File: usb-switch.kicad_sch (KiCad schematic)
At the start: 4 parts, among them U17 FSUSB42UMX

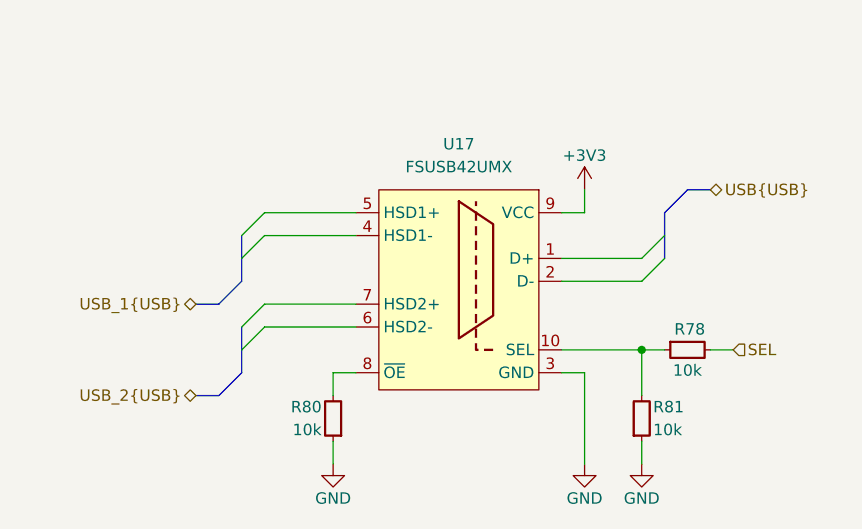
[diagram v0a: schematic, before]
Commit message: [#3] Layout HDMI, PCIe and ETH differential pairs
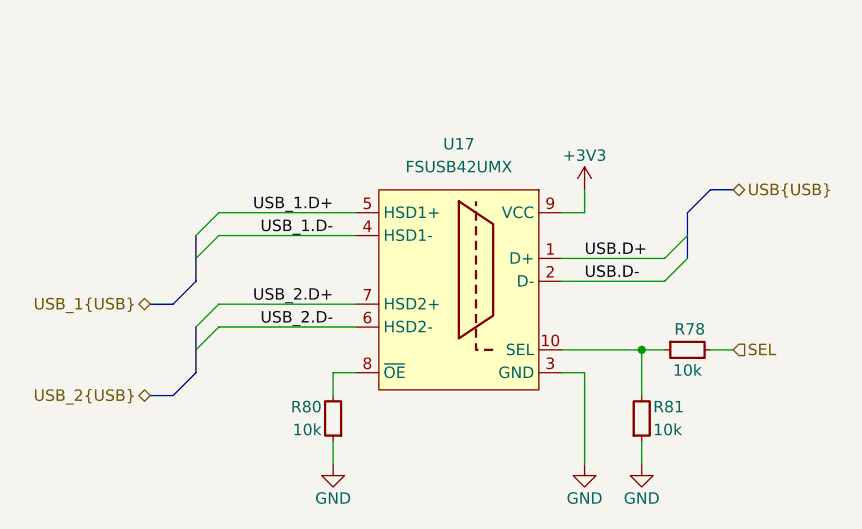
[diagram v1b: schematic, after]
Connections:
- net USB.D+: now reaches U17.1 (D+)
- net USB.D-: now reaches U17.2 (D-)
- net USB_1.D-: now reaches U17.4 (HSD1-)
- net USB_1.D+: now reaches U17.5 (HSD1+)
- net USB_2.D-: now reaches U17.6 (HSD2-)
- net USB_2.D+: now reaches U17.7 (HSD2+)
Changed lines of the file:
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@@
 	)
 	(bus_entry
-		(at 106.68 111.76)
+		(at 101.6 111.76)
 		(size 2.54 -2.54)
 		(stroke
@@
 	)
 	(bus_entry
-		(at 153.67 101.6)
+		(at 156.21 101.6)
 		(size -2.54 2.54)
 		(stroke
@@
 	)
 	(bus_entry
-		(at 153.67 104.14)
+		(at 156.21 104.14)
 		(size -2.54 2.54)
 		(stroke
@@
 	)
 	(bus_entry
-		(at 106.68 104.14)
+		(at 101.6 104.14)
 		(size 2.54 -2.54)
 		(stroke
@@
 	)
 	(bus_entry
-		(at 106.68 114.3)
+		(at 101.6 114.3)
 		(size 2.54 -2.54)
 		(stroke
@@
 	)
 	(bus_entry
-		(at 106.68 101.6)
+		(at 101.6 101.6)
 		(size 2.54 -2.54)
 		(stroke
@@
 	(bus
 		(pts
-			(xy 106.68 114.3) (xy 106.68 116.84)
-		)
-		(stroke
-			(width 0)
-			(type default)
-		)
-	)
-	(wire
-		(pts
-			(xy 142.24 106.68) (xy 151.13 106.68)
+			(xy 101.6 114.3) (xy 101.6 116.84)
+		)
+		(stroke
+			(width 0)
+			(type default)
+		)
+	)
+	(wire
+		(pts
+			(xy 142.24 106.68) (xy 153.67 106.68)
 		)
 		(stroke
@@
 	(wire
 		(pts
-			(xy 109.22 109.22) (xy 119.38 109.22)
-		)
-		(stroke
-			(width 0)
-			(type default)
-		)
-	)
-	(bus
-		(pts
-			(xy 106.68 104.14) (xy 106.68 106.68)
-		)
-		(stroke
-			(width 0)
-			(type default)
-		)
-	)
-	(bus
-		(pts
-			(xy 158.75 96.52) (xy 156.21 96.52)
-		)
-		(stroke
-			(width 0)
-			(type default)
-		)
-	)
-	(bus
-		(pts
-			(xy 106.68 101.6) (xy 106.68 104.14)
+			(xy 104.14 109.22) (xy 119.38 109.22)
+		)
+		(stroke
+			(width 0)
+			(type default)
+		)
+	)
+	(bus
+		(pts
+			(xy 161.29 96.52) (xy 158.75 96.52)
+		)
+		(stroke
+			(width 0)
+			(type default)
+		)
+	)
+	(bus
+		(pts
+			(xy 101.6 101.6) (xy 101.6 104.14)
 		)
 		(stroke
@@
 	(bus
 		(pts
-			(xy 101.6 119.38) (xy 104.14 119.38)
+			(xy 96.52 119.38) (xy 99.06 119.38)
 		)
 		(stroke
@@
 	(bus
 		(pts
-			(xy 101.6 109.22) (xy 104.14 109.22)
-		)
-		(stroke
-			(width 0)
-			(type default)
-		)
-	)
-	(bus
-		(pts
-			(xy 104.14 109.22) (xy 106.68 106.68)
-		)
-		(stroke
-			(width 0)
-			(type default)
-		)
-	)
-	(bus
-		(pts
-			(xy 104.14 119.38) (xy 106.68 116.84)
+			(xy 96.52 109.22) (xy 99.06 109.22)
+		)
+		(stroke
+			(width 0)
+			(type default)
+		)
+	)
+	(bus
+		(pts
+			(xy 99.06 109.22) (xy 101.6 106.68)
+		)
+		(stroke
+			(width 0)
+			(type default)
+		)
+	)
+	(bus
+		(pts
+			(xy 99.06 119.38) (xy 101.6 116.84)
 		)
 		(stroke
@@
 	(wire
 		(pts
-			(xy 109.22 111.76) (xy 119.38 111.76)
-		)
-		(stroke
-			(width 0)
-			(type default)
-		)
-	)
-	(bus
-		(pts
-			(xy 153.67 101.6) (xy 153.67 99.06)
-		)
-		(stroke
-			(width 0)
-			(type default)
-		)
-	)
-	(wire
-		(pts
-			(xy 142.24 104.14) (xy 151.13 104.14)
-		)
-		(stroke
-			(width 0)
-			(type default)
-		)
-	)
-	(wire
-		(pts
-			(xy 109.22 99.06) (xy 119.38 99.06)
-		)
-		(stroke
-			(width 0)
-			(type default)
-		)
-	)
-	(bus
-		(pts
-			(xy 153.67 104.14) (xy 153.67 101.6)
+			(xy 104.14 111.76) (xy 119.38 111.76)
+		)
+		(stroke
+			(width 0)
+			(type default)
+		)
+	)
+	(bus
+		(pts
+			(xy 156.21 101.6) (xy 156.21 99.06)
+		)
+		(stroke
+			(width 0)
+			(type default)
+		)
+	)
+	(wire
+		(pts
+			(xy 142.24 104.14) (xy 153.67 104.14)
+		)
+		(stroke
+			(width 0)
+			(type default)
+		)
+	)
+	(wire
+		(pts
+			(xy 104.14 99.06) (xy 119.38 99.06)
+		)
+		(stroke
+			(width 0)
+			(type default)
+		)
+	)
+	(bus
+		(pts
+			(xy 156.21 104.14) (xy 156.21 101.6)
+		)
+		(stroke
+			(width 0)
+			(type default)
+		)
+	)
+	(bus
+		(pts
+			(xy 101.6 104.14) (xy 101.6 106.68)
 		)
 		(stroke
@@
 	(bus
 		(pts
-			(xy 106.68 111.76) (xy 106.68 114.3)
-		)
-		(stroke
-			(width 0)
-			(type default)
-		)
-	)
-	(bus
-		(pts
-			(xy 156.21 96.52) (xy 153.67 99.06)
+			(xy 101.6 111.76) (xy 101.6 114.3)
+		)
+		(stroke
+			(width 0)
+			(type default)
+		)
+	)
+	(bus
+		(pts
+			(xy 158.75 96.52) (xy 156.21 99.06)
 		)
 		(stroke
@@
 	(wire
 		(pts
-			(xy 109.22 101.6) (xy 119.38 101.6)
+			(xy 104.14 101.6) (xy 119.38 101.6)
 		)
 		(stroke
@@
 			(width 0)
 			(type default)
+		)
+	)
+	(label "USB.D+"
+		(at 144.78 104.14 0)
+		(effects
+			(font
+				(size 1.27 1.27)
+			)
+			(justify left bottom)
+		)
+	)
+	(label "USB_1.D+"
+		(at 116.84 99.06 180)
+		(effects
+			(font
+				(size 1.27 1.27)
+			)
+			(justify right bottom)
+		)
+	)
+	(label "USB_1.D-"
+		(at 116.84 101.6 180)
+		(effects
+			(font
+				(size 1.27 1.27)
+			)
+			(justify right bottom)
+		)
+	)
+	(label "USB_2.D+"
+		(at 116.84 109.22 180)
+		(effects
+			(font
+				(size 1.27 1.27)
+			)
+			(justify right bottom)
+		)
+	)
+	(label "USB.D-"
+		(at 144.78 106.68 0)
+		(effects
+			(font
+				(size 1.27 1.27)
+			)
+			(justify left bottom)
+		)
+	)
+	(label "USB_2.D-"
+		(at 116.84 111.76 180)
+		(effects
+			(font
+				(size 1.27 1.27)
+			)
+			(justify right bottom)
 		)
 	)
 	(hierarchical_label "USB_1{USB}"
 		(shape bidirectional)
-		(at 101.6 109.22 180)
+		(at 96.52 109.22 180)
 		(effects
 			(font
@@
 	(hierarchical_label "USB_2{USB}"
 		(shape bidirectional)
-		(at 101.6 119.38 180)
+		(at 96.52 119.38 180)
 		(effects
 			(font
@@
 	(hierarchical_label "USB{USB}"
 		(shape bidirectional)
-		(at 158.75 96.52 0)
-		(effects
-			(font
+		(at 161.29 96.52 0)
+		(effects
+			(font

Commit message: [#3] Continue layout, minor schematic fixes, add power switch for CAN transceiver 5V rail
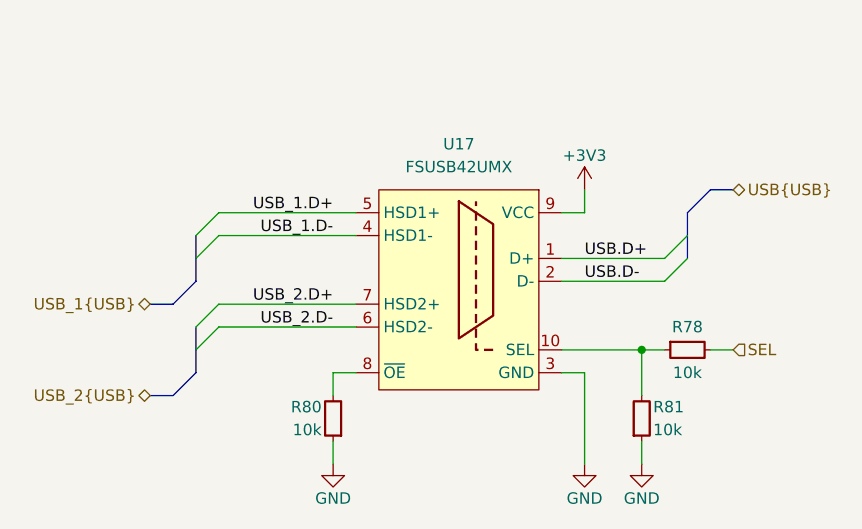
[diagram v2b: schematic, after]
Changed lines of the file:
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@@
 		(dnp no)
 		(property "Reference" "R78"
-			(at 156.464 112.014 0)
+			(at 156.21 111.76 0)
 			(effects
 				(font
@@
 		)
 		(property "Val" "10k"
-			(at 156.21 116.586 0)
+			(at 156.21 116.84 0)
 			(effects
 				(font

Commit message: [#3] WIP: Clear ERC, re-annotate schematic
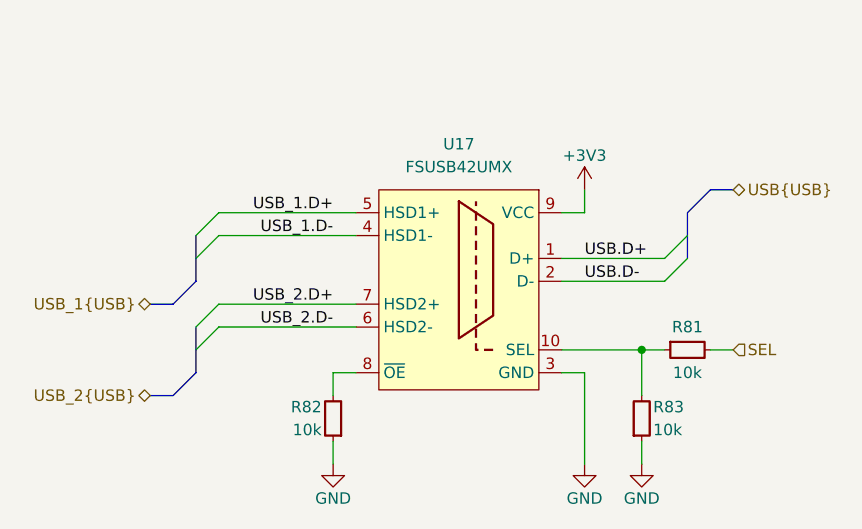
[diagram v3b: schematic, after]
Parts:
- renumbered R78 to R81, R80 to R82, R81 to R83
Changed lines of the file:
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@@
 		(on_board yes)
 		(dnp no)
-		(property "Reference" "#PWR0186"
+		(property "Reference" "#PWR0202"
 			(at 144.78 100.33 0)
 			(effects
@@
 			(project "cm5-module"
 				(path "/090a8e41-87a8-4fb1-998b-60a2c0dc4cee/68eae20e-0e1b-4ef5-aecc-d5a324940476"
-					(reference "#PWR0186")
+					(reference "#PWR0202")
 					(unit 1)
 				)
@@
 		(on_board yes)
 		(dnp no)
-		(property "Reference" "R78"
+		(property "Reference" "R81"
 			(at 156.21 111.76 0)
 			(effects
@@
 			(project ""
 				(path "/090a8e41-87a8-4fb1-998b-60a2c0dc4cee/68eae20e-0e1b-4ef5-aecc-d5a324940476"
-					(reference "R78")
+					(reference "R81")
 					(unit 1)
 				)
@@
 		(on_board yes)
 		(dnp no)
-		(property "Reference" "R81"
+		(property "Reference" "R83"
 			(at 152.4 120.65 90)
 			(effects
@@
 			(project "cm5-module"
 				(path "/090a8e41-87a8-4fb1-998b-60a2c0dc4cee/68eae20e-0e1b-4ef5-aecc-d5a324940476"
-					(reference "R81")
+					(reference "R83")
 					(unit 1)
 				)
@@
 		(on_board yes)
 		(dnp no)
-		(property "Reference" "#PWR0190"
+		(property "Reference" "#PWR0205"
 			(at 151.13 133.35 0)
 			(effects
@@
 			(project "cm5-module"
 				(path "/090a8e41-87a8-4fb1-998b-60a2c0dc4cee/68eae20e-0e1b-4ef5-aecc-d5a324940476"
-					(reference "#PWR0190")
+					(reference "#PWR0205")
 					(unit 1)
 				)
@@
 		(on_board yes)
 		(dnp no)
-		(property "Reference" "#PWR0185"
+		(property "Reference" "#PWR0204"
 			(at 144.78 133.35 0)
 			(effects
@@
 			(project "cm5-module"
 				(path "/090a8e41-87a8-4fb1-998b-60a2c0dc4cee/68eae20e-0e1b-4ef5-aecc-d5a324940476"
-					(reference "#PWR0185")
+					(reference "#PWR0204")
 					(unit 1)
 				)
@@
 		(on_board yes)
 		(dnp no)
-		(property "Reference" "R80"
+		(property "Reference" "R82"
 			(at 115.57 120.65 90)
 			(effects
@@
 			(project "cm5-module"
 				(path "/090a8e41-87a8-4fb1-998b-60a2c0dc4cee/68eae20e-0e1b-4ef5-aecc-d5a324940476"
-					(reference "R80")
+					(reference "R82")
 					(unit 1)
 				)
@@
 		(on_board yes)
 		(dnp no)
-		(property "Reference" "#PWR0189"
+		(property "Reference" "#PWR0203"
 			(at 116.84 133.35 0)
 			(effects
@@
 			(project "cm5-module"
 				(path "/090a8e41-87a8-4fb1-998b-60a2c0dc4cee/68eae20e-0e1b-4ef5-aecc-d5a324940476"
-					(reference "#PWR0189")
+					(reference "#PWR0203")
 					(unit 1)
 				)

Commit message: [#3] Start USB layout
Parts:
- added C80: C-100n-0402, DW-footprints:C_0402_1005Metric, symbol DW-capacitors:C-100n-0402
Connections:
- net +3V3: now also C80.2
- net GND: now also C80.1

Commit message: [#3] Re-annotate schematic
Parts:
- renumbered C80 to C59, R81 to R64, R82 to R65, R83 to R66, U17 to U12
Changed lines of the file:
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@@
 		(on_board yes)
 		(dnp no)
-		(property "Reference" "#PWR0202"
+		(property "Reference" "#PWR0138"
 			(at 151.13 86.36 0)
 			(effects
@@
 			(project "cm5-module"
 				(path "/090a8e41-87a8-4fb1-998b-60a2c0dc4cee/68eae20e-0e1b-4ef5-aecc-d5a324940476"
-					(reference "#PWR0202")
+					(reference "#PWR0138")
 					(unit 1)
 				)
@@
 		(on_board yes)
 		(dnp no)
-		(property "Reference" "C80"
+		(property "Reference" "C59"
 			(at 153.67 88.8936 90)
 			(effects
@@
 			(project "cm5-module"
 				(path "/090a8e41-87a8-4fb1-998b-60a2c0dc4cee/68eae20e-0e1b-4ef5-aecc-d5a324940476"
-					(reference "C80")
+					(reference "C59")
 					(unit 1)
 				)
@@
 		(on_board yes)
 		(dnp no)
-		(property "Reference" "R81"
+		(property "Reference" "R64"
 			(at 156.21 111.76 0)
 			(effects
@@
 			(project ""
 				(path "/090a8e41-87a8-4fb1-998b-60a2c0dc4cee/68eae20e-0e1b-4ef5-aecc-d5a324940476"
-					(reference "R81")
+					(reference "R64")
 					(unit 1)
 				)
@@
 		(on_board yes)
 		(dnp no)
-		(property "Reference" "R83"
+		(property "Reference" "R66"
 			(at 152.4 120.65 90)
 			(effects
@@
 			(project "cm5-module"
 				(path "/090a8e41-87a8-4fb1-998b-60a2c0dc4cee/68eae20e-0e1b-4ef5-aecc-d5a324940476"
-					(reference "R83")
+					(reference "R66")
 					(unit 1)
 				)
@@
 		(on_board yes)
 		(dnp no)
-		(property "Reference" "#PWR0205"
+		(property "Reference" "#PWR0142"
 			(at 151.13 133.35 0)
 			(effects
@@
 			(project "cm5-module"
 				(path "/090a8e41-87a8-4fb1-998b-60a2c0dc4cee/68eae20e-0e1b-4ef5-aecc-d5a324940476"
-					(reference "#PWR0205")
+					(reference "#PWR0142")
 					(unit 1)
 				)
@@
 		(dnp no)
 		(fields_autoplaced yes)
-		(property "Reference" "U17"
+		(property "Reference" "U12"
 			(at 130.81 91.44 0)
 			(effects
@@
 			(project ""
 				(path "/090a8e41-87a8-4fb1-998b-60a2c0dc4cee/68eae20e-0e1b-4ef5-aecc-d5a324940476"
-					(reference "U17")
+					(reference "U12")
 					(unit 1)
 				)
@@
 		(on_board yes)
 		(dnp no)
-		(property "Reference" "#PWR0204"
+		(property "Reference" "#PWR0141"
 			(at 144.78 133.35 0)
 			(effects
@@
 			(project "cm5-module"
 				(path "/090a8e41-87a8-4fb1-998b-60a2c0dc4cee/68eae20e-0e1b-4ef5-aecc-d5a324940476"
-					(reference "#PWR0204")
+					(reference "#PWR0141")
 					(unit 1)
 				)
@@
 		(on_board yes)
 		(dnp no)
-		(property "Reference" "R82"
+		(property "Reference" "R65"
 			(at 115.57 120.65 90)
 			(effects
@@
 			(project "cm5-module"
 				(path "/090a8e41-87a8-4fb1-998b-60a2c0dc4cee/68eae20e-0e1b-4ef5-aecc-d5a324940476"
-					(reference "R82")
+					(reference "R65")
 					(unit 1)
 				)
@@
 		(on_board yes)
 		(dnp no)
-		(property "Reference" "#PWR0203"
+		(property "Reference" "#PWR0140"
 			(at 116.84 133.35 0)
 			(effects
@@
 			(project "cm5-module"
 				(path "/090a8e41-87a8-4fb1-998b-60a2c0dc4cee/68eae20e-0e1b-4ef5-aecc-d5a324940476"
-					(reference "#PWR0203")
+					(reference "#PWR0140")
 					(unit 1)
 				)
@@
 		(on_board yes)
 		(dnp no)
-		(property "Reference" "#PWR017"
+		(property "Reference" "#PWR0139"
 			(at 151.13 101.6 0)
 			(effects
@@
 			(project "cm5-module"
 				(path "/090a8e41-87a8-4fb1-998b-60a2c0dc4cee/68eae20e-0e1b-4ef5-aecc-d5a324940476"
-					(reference "#PWR017")
+					(reference "#PWR0139")
 					(unit 1)
 				)
